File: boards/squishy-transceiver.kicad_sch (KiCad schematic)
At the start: 99 parts, among them Q2 Q_PMOS_DGS, Q3 Q_DUAL_PMOS_S1G1D2S2G2D1, Q4 Q_DUAL_PMOS_S1G1D2S2G2D1, U1 THVD1452DGSR, U10 THVD1452DGSR, U11 FXL4TD245BQX, U13 THVD1452DGSR, U15 THVD1452DGSR, U16 FXL4TD245BQX, U17 THVD1452DGSR, U18 THVD1452DGSR, U2 FXL4TD245BQX, U20 FXL4TD245BQX, U21 THVD1452DGSR, U22 THVD1452DGSR, U23 FXL4TD245BQX, U24 THVD1452DGSR, U25 THVD1452DGSR, U27 FXL4TD245BQX, U28 THVD1452DGSR, U29 THVD1452DGSR, U30 FXL4TD245BQX, U31 THVD1452DGSR, U32 THVD1452DGSR, U33 FXL4TD245BQX, U34 THVD1452DGSR, U4 THVD1452DGSR, U6 THVD1452DGSR, U8 FXL4TD245BQX, U9 THVD1452DGSR

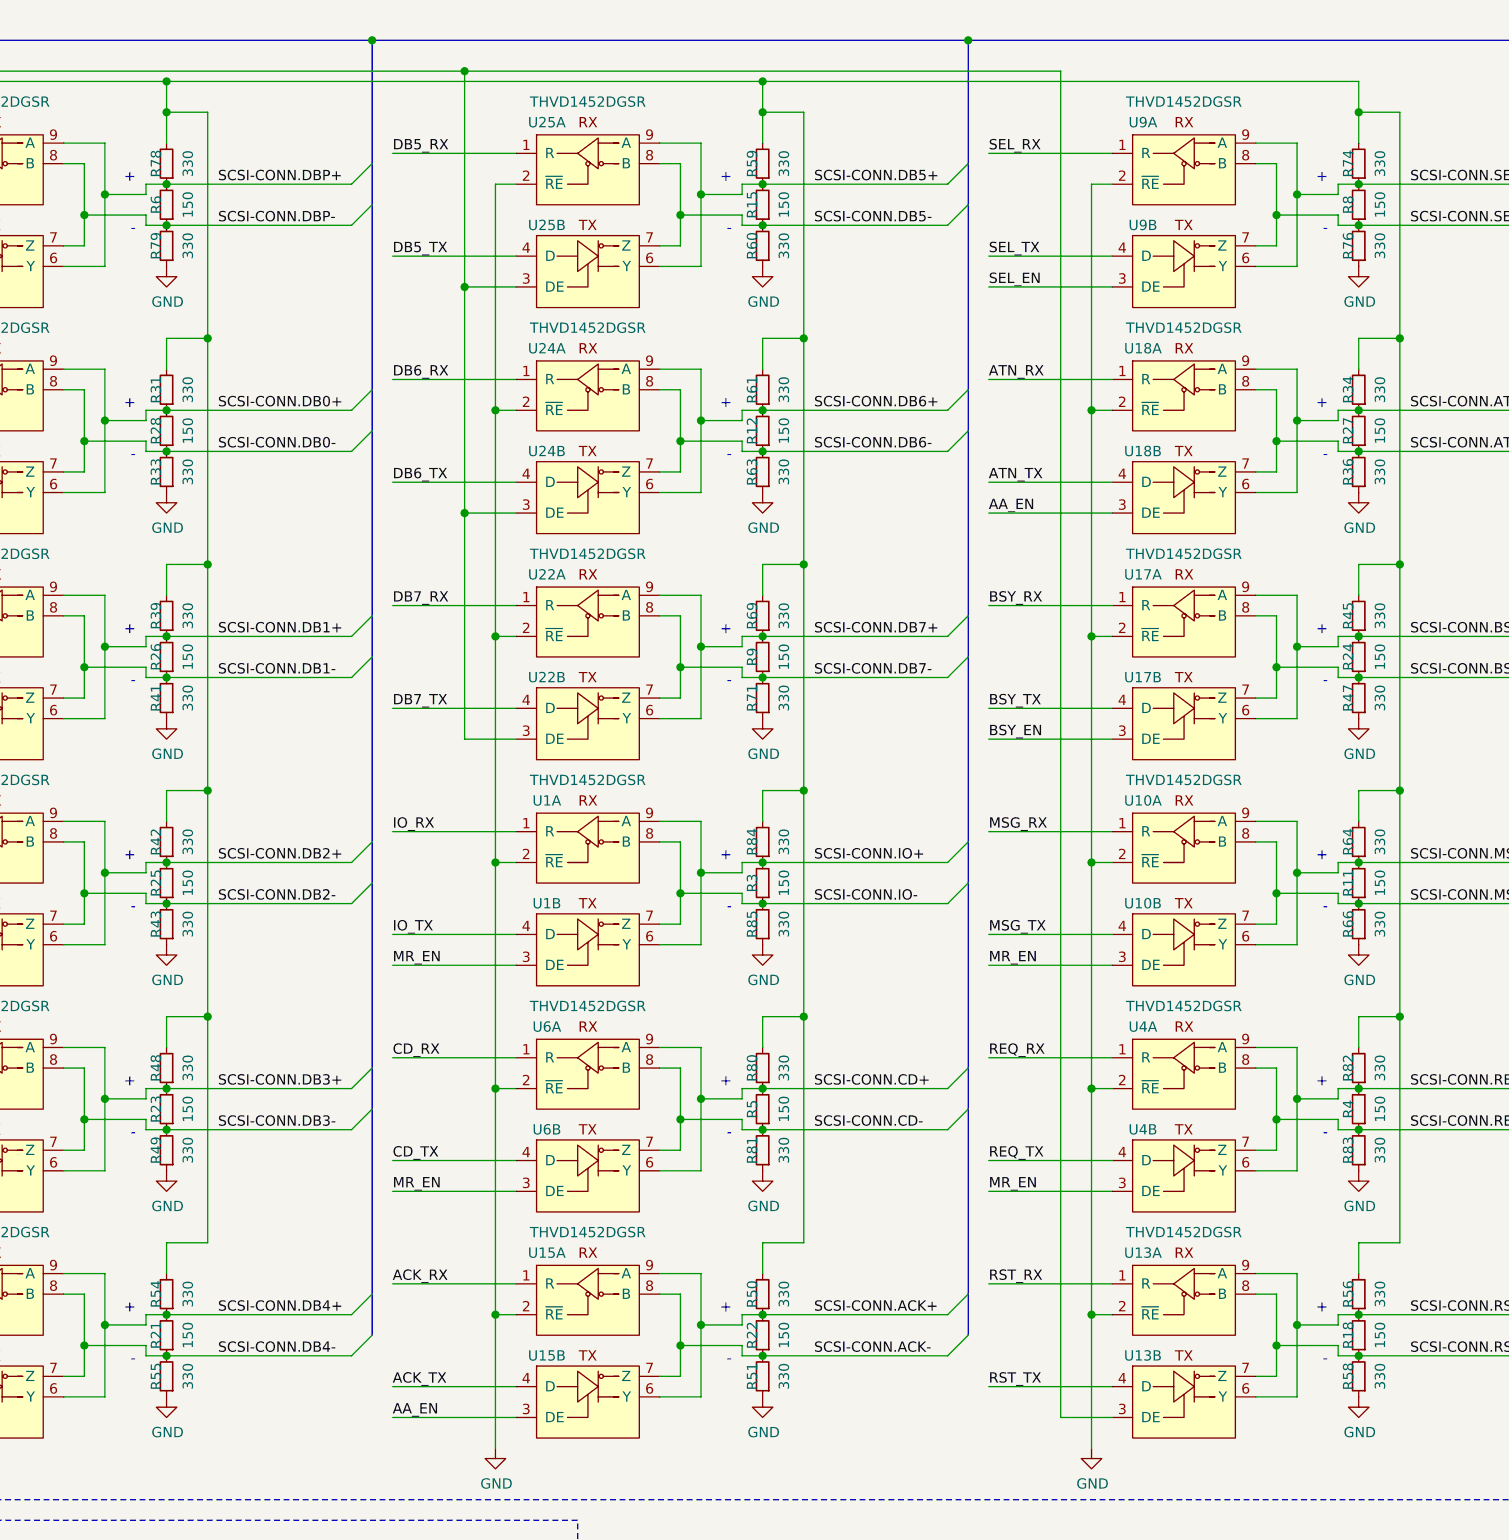
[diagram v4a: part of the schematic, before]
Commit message: hardware: termination resistors kicked my ass, but most of the nets are correct now
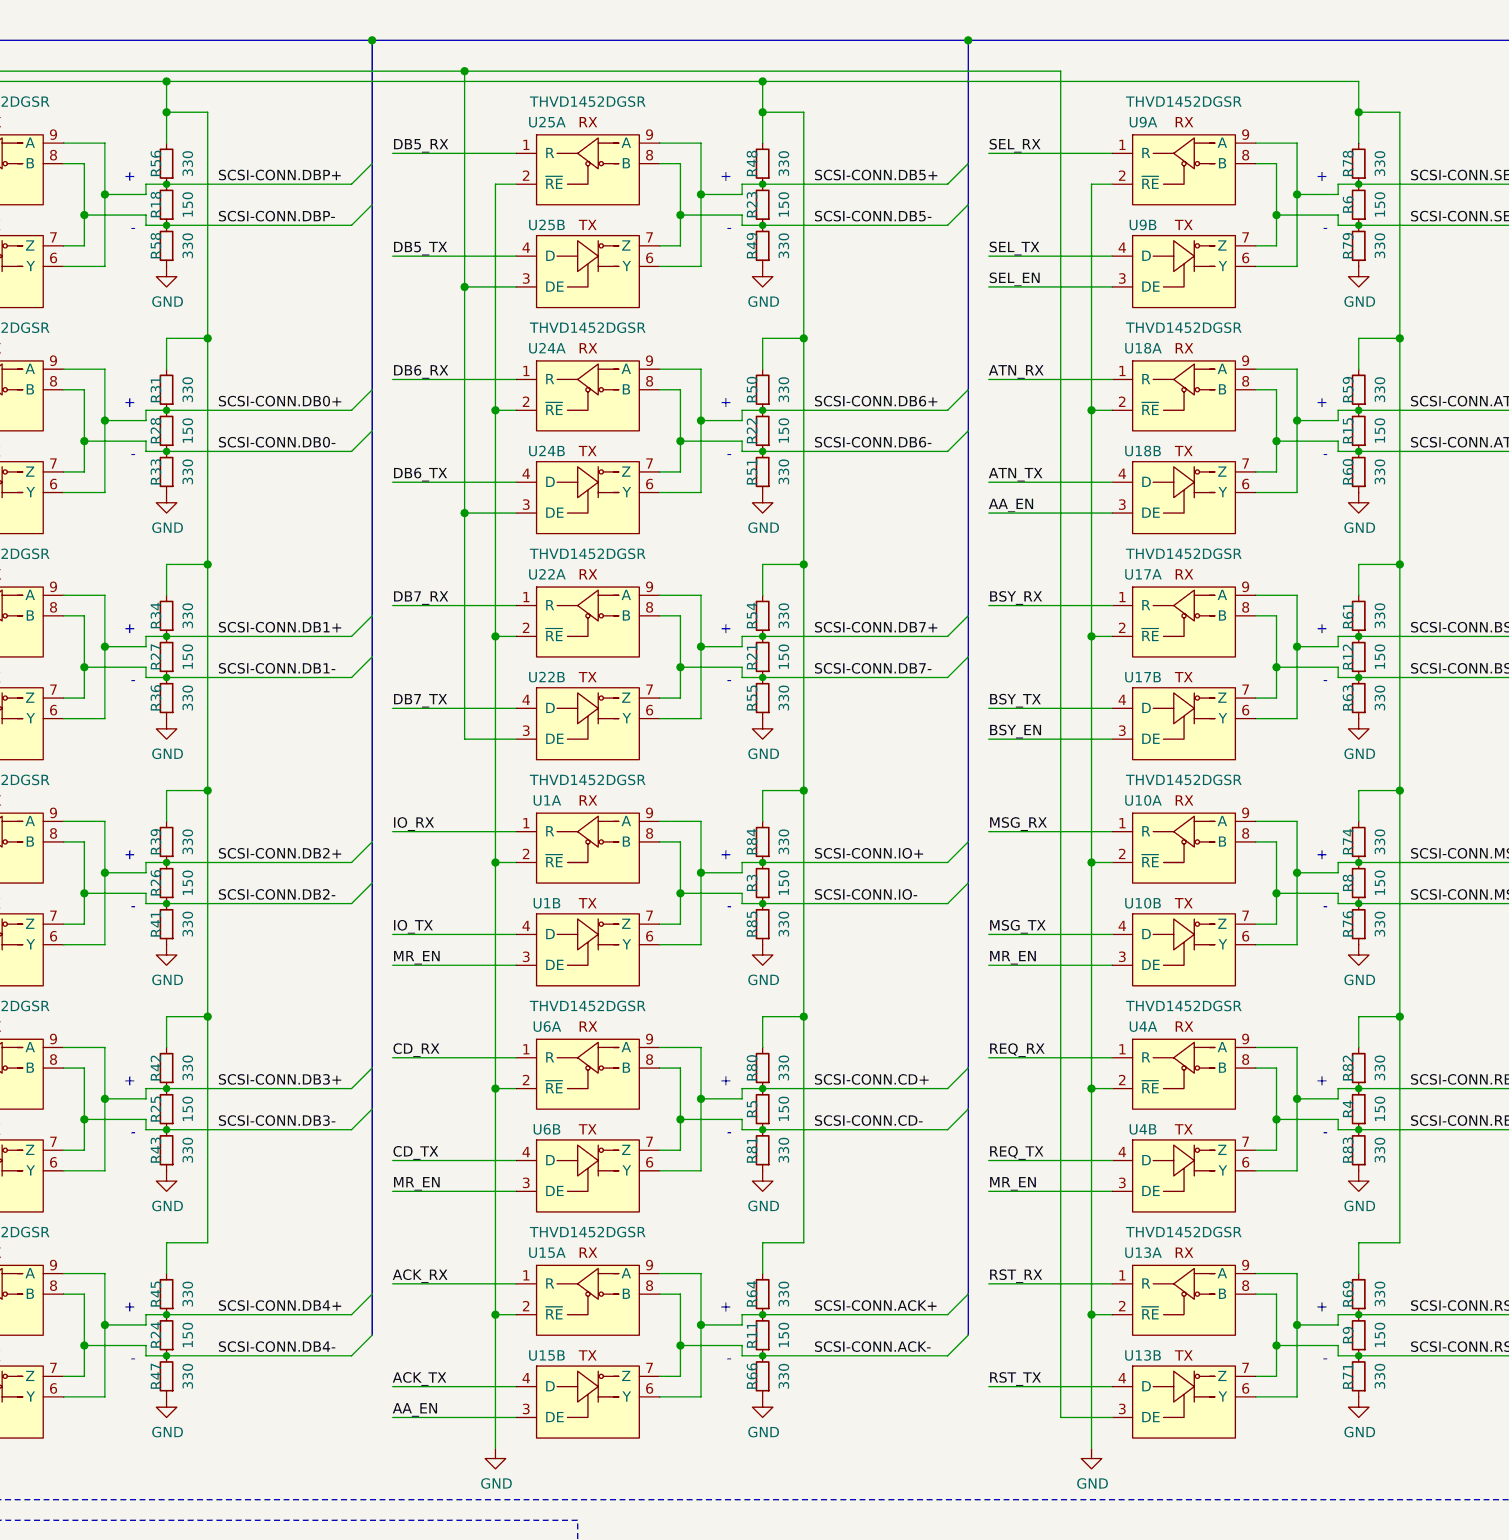
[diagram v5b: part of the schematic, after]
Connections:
- net SCSI-CONN.ACK+: now also R11.2, R64.1; no longer R22.2, R50.1
- net SCSI-CONN.ACK-: now also R11.1, R66.2; no longer R22.1, R51.2
- net SCSI-CONN.ATN+: now also R15.2, R59.1; no longer R27.2, R34.1
- net SCSI-CONN.ATN-: now also R15.1, R60.2; no longer R27.1, R36.2
- net SCSI-CONN.BSY+: now also R12.2, R61.1; no longer R24.2, R45.1
- net SCSI-CONN.BSY-: now also R12.1, R63.2; no longer R24.1, R47.2
- net SCSI-CONN.DB1+: now also R27.2, R34.1; no longer R26.2, R39.1
- net SCSI-CONN.DB1-: now also R27.1, R36.2; no longer R26.1, R41.2
- net SCSI-CONN.DB2+: now also R26.2, R39.1; no longer R25.2, R42.1
- net SCSI-CONN.DB2-: now also R26.1, R41.2; no longer R25.1, R43.2
- net SCSI-CONN.DB3+: now also R25.2, R42.1; no longer R23.2, R48.1
- net SCSI-CONN.DB3-: now also R25.1, R43.2; no longer R23.1, R49.2
- net SCSI-CONN.DB4+: now also R24.2, R45.1; no longer R21.2, R54.1
- net SCSI-CONN.DB4-: now also R24.1, R47.2; no longer R21.1, R55.2
- net SCSI-CONN.DB5+: now also R23.2, R48.1; no longer R15.2, R59.1
- net SCSI-CONN.DB5-: now also R23.1, R49.2; no longer R15.1, R60.2
- net SCSI-CONN.DB6+: now also R22.2, R50.1; no longer R12.2, R61.1
- net SCSI-CONN.DB6-: now also R22.1, R51.2; no longer R12.1, R63.2
- net SCSI-CONN.DB7+: now also R21.2, R54.1; no longer R69.1, R9.2
- net SCSI-CONN.DB7-: now also R21.1, R55.2; no longer R71.2, R9.1
- net SCSI-CONN.DBP+: now also R18.2, R56.1; no longer R6.2, R78.1
- net SCSI-CONN.DBP-: now also R18.1, R58.2; no longer R6.1, R79.2
- net SCSI-CONN.MSG+: now also R74.1, R8.2; no longer R11.2, R64.1
- net SCSI-CONN.MSG-: now also R76.2, R8.1; no longer R11.1, R66.2
- net SCSI-CONN.RST+: now also R69.1, R9.2; no longer R18.2, R56.1
- net SCSI-CONN.RST-: now also R71.2, R9.1; no longer R18.1, R58.2
- net SCSI-CONN.SEL+: now also R6.2, R78.1; no longer R74.1, R8.2
- net SCSI-CONN.SEL-: now also R6.1, R79.2; no longer R76.2, R8.1
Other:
- moved on the sheet: R11, R12, R15, R18, R21, R22, R23, R24, R25, R26, R27, R34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

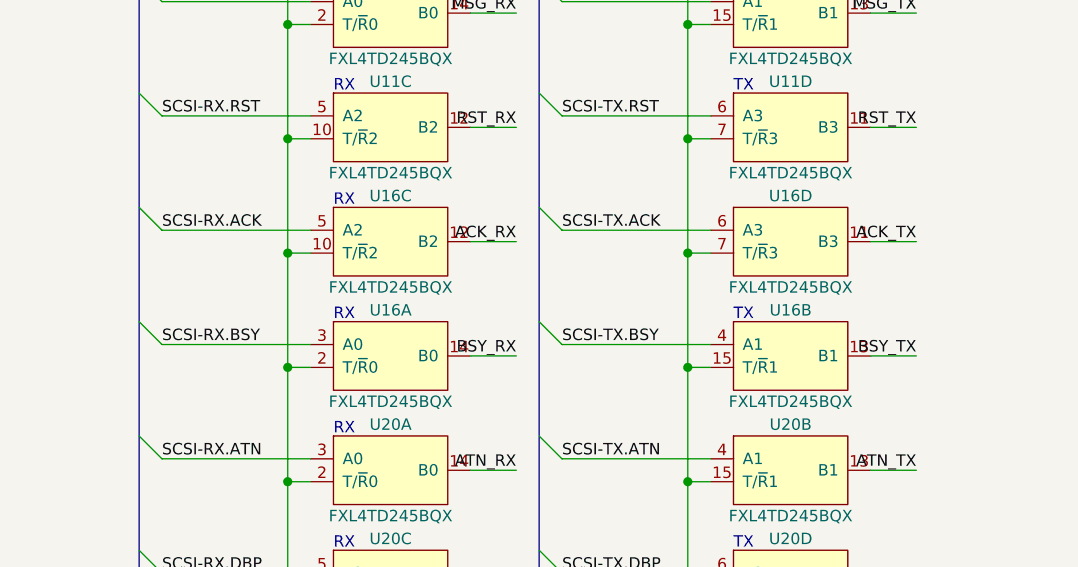
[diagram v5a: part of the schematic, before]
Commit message: hardware: fixed up the bsy/ack as they were mixed up, still need to fix the enable signals
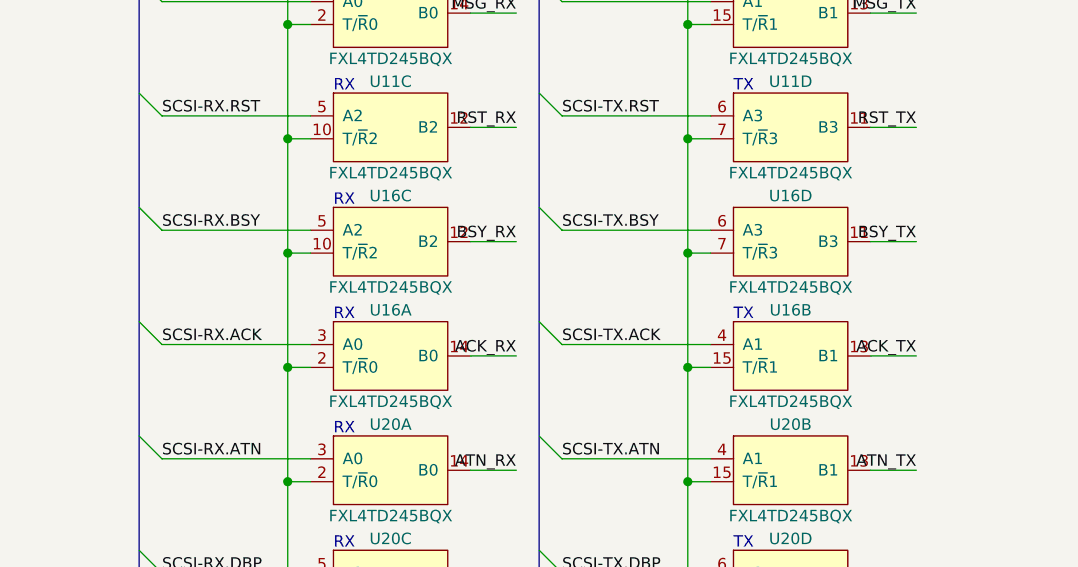
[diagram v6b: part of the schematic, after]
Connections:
- net ACK_RX: now also U16.14 (B0); no longer U16.12 (B2)
- net ACK_TX: now also U16.13 (B1); no longer U16.11 (B3)
- net BSY_RX: now also U16.12 (B2); no longer U16.14 (B0)
- net BSY_TX: now also U16.11 (B3); no longer U16.13 (B1)
- net SCSI-RX.ACK: now also U16.3 (A0); no longer U16.5 (A2)
- net SCSI-RX.BSY: now also U16.5 (A2); no longer U16.3 (A0)
- net SCSI-TX.ACK: now also U16.4 (A1); no longer U16.6 (A3)
- net SCSI-TX.BSY: now also U16.6 (A3); no longer U16.4 (A1)
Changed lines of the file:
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@@
     (effects (font (size 1.27 1.27)) (justify left bottom))
   )
-  (label "SCSI-RX.ACK" (at 49.53 107.95 0)
+  (label "SCSI-RX.BSY" (at 49.53 107.95 0)
     (effects (font (size 1.27 1.27)) (justify left bottom))
   )
-  (label "SCSI-RX.BSY" (at 49.53 120.65 0)
+  (label "SCSI-RX.ACK" (at 49.53 120.65 0)
     (effects (font (size 1.27 1.27)) (justify left bottom))
   )
@@
     (effects (font (size 1.27 1.27)) (justify right bottom))
   )
-  (label "ACK_RX" (at 88.9 109.22 180)
+  (label "BSY_RX" (at 88.9 109.22 180)
     (effects (font (size 1.27 1.27)) (justify right bottom))
   )
-  (label "BSY_RX" (at 88.9 121.92 180)
+  (label "ACK_RX" (at 88.9 121.92 180)
     (effects (font (size 1.27 1.27)) (justify right bottom))
   )
@@
     (effects (font (size 1.27 1.27)) (justify left bottom))
   )
-  (label "SCSI-TX.ACK" (at 93.98 107.95 0)
+  (label "SCSI-TX.BSY" (at 93.98 107.95 0)
     (effects (font (size 1.27 1.27)) (justify left bottom))
   )
-  (label "SCSI-TX.BSY" (at 93.98 120.65 0)
+  (label "SCSI-TX.ACK" (at 93.98 120.65 0)
     (effects (font (size 1.27 1.27)) (justify left bottom))
   )
@@
     (effects (font (size 1.27 1.27)) (justify right bottom))
   )
-  (label "ACK_TX" (at 133.35 109.22 180)
+  (label "BSY_TX" (at 133.35 109.22 180)
     (effects (font (size 1.27 1.27)) (justify right bottom))
   )
-  (label "BSY_TX" (at 133.35 121.92 180)
+  (label "ACK_TX" (at 133.35 121.92 180)
     (effects (font (size 1.27 1.27)) (justify right bottom))
   )
